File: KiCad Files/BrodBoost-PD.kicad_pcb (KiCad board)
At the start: 4 copper layers, 54 x 11.6 mm, 39 parts, among them IC1 CYPD3177, J1 Conn_02x02_Counter_Clockwise, J2 Conn_02x02_Counter_Clockwise, J4 Conn_01x02_Pin, J6 Output, P1 USB Type C, Q2 DMP3013, Q3 DMP3013, SW1 SW_DIP_x05

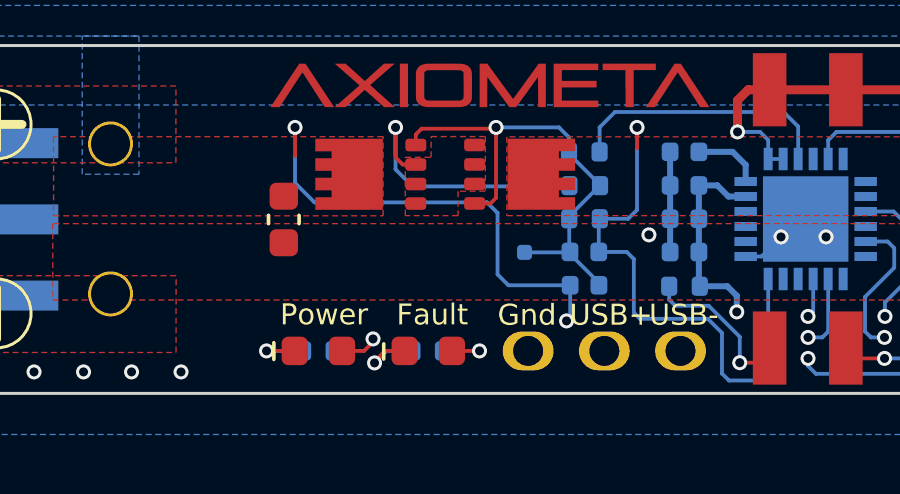
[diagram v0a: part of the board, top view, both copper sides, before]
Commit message: almost finished husb238 version
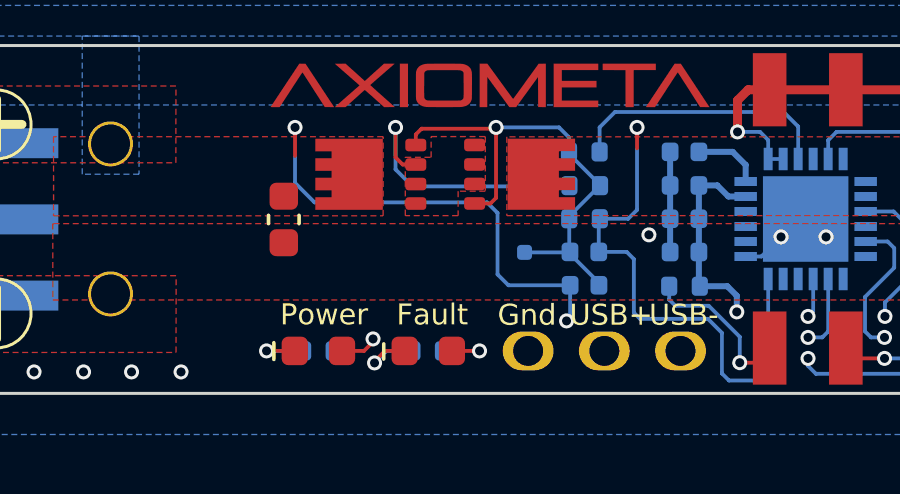
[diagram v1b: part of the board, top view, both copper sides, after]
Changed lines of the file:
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@@
 	)
 	(gr_text "Fault"
-		(at 145.684178 106.94975 0)
+		(at 145.683178 106.94975 0)
 		(layer "F.SilkS")
 		(effects
@@
 			(polygon
 				(pts
-					(xy 145.757438 106.83075) (xy 145.757438 106.144732) (xy 146.174904 106.144732) (xy 146.174904 106.212351)
-					(xy 145.83976 106.212351) (xy 145.83976 106.453461) (xy 146.124938 106.453461) (xy 146.124938 106.520097)
-					(xy 145.83976 106.520097) (xy 145.83976 106.83075)
+					(xy 145.756438 106.83075) (xy 145.756438 106.144732) (xy 146.173904 106.144732) (xy 146.173904 106.212351)
+					(xy 145.83876 106.212351) (xy 145.83876 106.453461) (xy 146.123938 106.453461) (xy 146.123938 106.520097)
+					(xy 145.83876 106.520097) (xy 145.83876 106.83075)
 				)
 			)
 			(polygon
 				(pts
-					(xy 146.489112 106.328633) (xy 146.526534 106.337184) (xy 146.557791 106.35058) (xy 146.58581 106.369598)
-					(xy 146.608342 106.392654) (xy 146.625923 106.420122) (xy 146.638219 106.450617) (xy 146.645892 106.485245)
-					(xy 146.648576 106.524756) (xy 146.648576 106.83075) (xy 146.575102 106.83075) (xy 146.570187 106.743298)
-					(xy 146.559099 106.763159) (xy 146.545182 106.78198) (xy 146.528802 106.798869) (xy 146.509792 106.813482)
-					(xy 146.488409 106.825273) (xy 146.463245 106.834639) (xy 146.435958 106.840448) (xy 146.404089 106.842504)
-					(xy 146.364321 106.839929) (xy 146.331287 106.832749) (xy 146.303858 106.82156) (xy 146.278998 106.805655)
-					(xy 146.259361 106.787087) (xy 146.244318 106.765695) (xy 146.229654 106.729414) (xy 146.224742 106.690127)
-					(xy 146.22511 106.686194) (xy 146.310996 106.686194) (xy 146.314118 106.711116) (xy 146.323092 106.732014)
-					(xy 146.337866 106.749159) (xy 146.358996 106.762276) (xy 146.38431 106.770077) (xy 146.41657 106.772919)
-					(xy 146.449807 106.769252) (xy 146.478932 106.7586) (xy 146.504705 106.741724) (xy 146.526461 106.719662)
-					(xy 146.543714 106.693581) (xy 146.55621 106.664396) (xy 146.563733 106.633272) (xy 146.566254 106.600923)
-					(xy 146.566254 106.59776) (xy 146.442558 106.59776) (xy 146.3975 106.600934) (xy 146.365749 106.609172)
-					(xy 146.339845 106.623264) (xy 146.323734 106.640503) (xy 146.314247 106.66167) (xy 146.310996 106.686194)
-					(xy 146.22511 106.686194) (xy 146.227793 106.657509) (xy 146.236518 106.629517) (xy 146.250687 106.60524)
-					(xy 146.269869 106.584416) (xy 146.294064 106.566784) (xy 146.324075 106.552325) (xy 146.37404 106.538912)
-					(xy 146.435676 106.534074) (xy 146.566254 106.534074) (xy 146.562467 106.490063) (xy 146.552278 106.457009)
-					(xy 146.534836 106.429819) (xy 146.511159 106.410676) (xy 146.481851 106.399246) (xy 146.444267 106.395118)
-					(xy 146.41363 106.397861) (xy 146.386741 106.405766) (xy 146.362886 106.418669) (xy 146.343166 106.43653)
-					(xy 146.329199 106.459111) (xy 146.320784 106.487484) (xy 146.236496 106.487484) (xy 146.24331 106.453654)
-					(xy 146.255268 106.424476) (xy 146.272272 106.399178) (xy 146.293785 106.377289) (xy 146.318875 106.35908)
-					(xy 146.347968 106.344425) (xy 146.394844 106.33031) (xy 146.444267 106.325576)
+					(xy 146.488112 106.328633) (xy 146.525534 106.337184) (xy 146.556791 106.35058) (xy 146.58481 106.369598)
+					(xy 146.607342 106.392654) (xy 146.624923 106.420122) (xy 146.637219 106.450617) (xy 146.644892 106.485245)
+					(xy 146.647576 106.524756) (xy 146.647576 106.83075) (xy 146.574102 106.83075) (xy 146.569187 106.743298)
+					(xy 146.558099 106.763159) (xy 146.544182 106.78198) (xy 146.527802 106.798869) (xy 146.508792 106.813482)
+					(xy 146.487409 106.825273) (xy 146.462245 106.834639) (xy 146.434958 106.840448) (xy 146.403089 106.842504)
+					(xy 146.363321 106.839929) (xy 146.330287 106.832749) (xy 146.302858 106.82156) (xy 146.277998 106.805655)
+					(xy 146.258361 106.787087) (xy 146.243318 106.765695) (xy 146.228654 106.729414) (xy 146.223742 106.690127)
+					(xy 146.22411 106.686194) (xy 146.309996 106.686194) (xy 146.313118 106.711116) (xy 146.322092 106.732014)
+					(xy 146.336866 106.749159) (xy 146.357996 106.762276) (xy 146.38331 106.770077) (xy 146.41557 106.772919)
+					(xy 146.448807 106.769252) (xy 146.477932 106.7586) (xy 146.503705 106.741724) (xy 146.525461 106.719662)
+					(xy 146.542714 106.693581) (xy 146.55521 106.664396) (xy 146.562733 106.633272) (xy 146.565254 106.600923)
+					(xy 146.565254 106.59776) (xy 146.441558 106.59776) (xy 146.3965 106.600934) (xy 146.364749 106.609172)
+					(xy 146.338845 106.623264) (xy 146.322734 106.640503) (xy 146.313247 106.66167) (xy 146.309996 106.686194)
+					(xy 146.22411 106.686194) (xy 146.226793 106.657509) (xy 146.235518 106.629517) (xy 146.249687 106.60524)
+					(xy 146.268869 106.584416) (xy 146.293064 106.566784) (xy 146.323075 106.552325) (xy 146.37304 106.538912)
+					(xy 146.434676 106.534074) (xy 146.565254 106.534074) (xy 146.561467 106.490063) (xy 146.551278 106.457009)
+					(xy 146.533836 106.429819) (xy 146.510159 106.410676) (xy 146.480851 106.399246) (xy 146.443267 106.395118)
+					(xy 146.41263 106.397861) (xy 146.385741 106.405766) (xy 146.361886 106.418669) (xy 146.342166 106.43653)
+					(xy 146.328199 106.459111) (xy 146.319784 106.487484) (xy 146.235496 106.487484) (xy 146.24231 106.453654)
+					(xy 146.254268 106.424476) (xy 146.271272 106.399178) (xy 146.292785 106.377289) (xy 146.317875 106.35908)
+					(xy 146.346968 106.344425) (xy 146.393844 106.33031) (xy 146.443267 106.325576)
 				)
 			)
 			(polygon
 				(pts
-					(xy 146.954698 106.842504) (xy 146.917387 106.839835) (xy 146.884511 106.83218) (xy 146.855365 106.81985)
-					(xy 146.829401 106.802267) (xy 146.807601 106.77935) (xy 146.789669 106.750394) (xy 146.777354 106.718358)
-					(xy 146.769407 106.679527) (xy 146.766546 106.632553) (xy 146.766546 106.33733) (xy 146.848868 106.33733)
-					(xy 146.848868 106.623705) (xy 146.853035 106.672157) (xy 146.864211 106.708251) (xy 146.881181 106.734878)
-					(xy 146.905047 106.755015) (xy 146.93512 106.767474) (xy 146.973291 106.771936) (xy 147.012741 106.766862)
-					(xy 147.047449 106.751975) (xy 147.067622 106.736895) (xy 147.084926 106.717739) (xy 147.09951 106.693974)
-					(xy 147.10977 106.667907) (xy 147.116295 106.637183) (xy 147.118616 106.600923) (xy 147.118616 106.33733)
-					(xy 147.200938 106.33733) (xy 147.200938 106.83075) (xy 147.126438 106.83075) (xy 147.121565 106.744752)
-					(xy 147.103949 106.773171) (xy 147.081786 106.796963) (xy 147.054673 106.816559) (xy 147.024341 106.830835)
-					(xy 146.991225 106.839522)
+					(xy 146.953698 106.842504) (xy 146.916387 106.839835) (xy 146.883511 106.83218) (xy 146.854365 106.81985)
+					(xy 146.828401 106.802267) (xy 146.806601 106.77935) (xy 146.788669 106.750394) (xy 146.776354 106.718358)
+					(xy 146.768407 106.679527) (xy 146.765546 106.632553) (xy 146.765546 106.33733) (xy 146.847868 106.33733)
+					(xy 146.847868 106.623705) (xy 146.852035 106.672157) (xy 146.863211 106.708251) (xy 146.880181 106.734878)
+					(xy 146.904047 106.755015) (xy 146.93412 106.767474) (xy 146.972291 106.771936) (xy 147.011741 106.766862)
+					(xy 147.046449 106.751975) (xy 147.066622 106.736895) (xy 147.083926 106.717739) (xy 147.09851 106.693974)
+					(xy 147.10877 106.667907) (xy 147.115295 106.637183) (xy 147.117616 106.600923) (xy 147.117616 106.33733)
+					(xy 147.199938 106.33733) (xy 147.199938 106.83075) (xy 147.125438 106.83075) (xy 147.120565 106.744752)
+					(xy 147.102949 106.773171) (xy 147.080786 106.796963) (xy 147.053673 106.816559) (xy 147.023341 106.830835)
+					(xy 146.990225 106.839522)
 				)
 			)
 			(polygon
 				(pts
-					(xy 147.336859 106.83075) (xy 147.336859 106.125156) (xy 147.419138 106.125156) (xy 147.419138 106.83075)
+					(xy 147.335859 106.83075) (xy 147.335859 106.125156) (xy 147.418138 106.125156) (xy 147.418138 106.83075)
 				)
 			)
 			(polygon
 				(pts
-					(xy 147.749025 106.83075) (xy 147.70675 106.827118) (xy 147.672559 106.817029) (xy 147.652787 106.805821)
-					(xy 147.636416 106.790479) (xy 147.623105 106.770483) (xy 147.614124 106.74791) (xy 147.608164 106.718853)
-					(xy 147.605966 106.681792) (xy 147.605966 106.406915) (xy 147.520224 106.406915) (xy 147.520224 106.33733)
-					(xy 147.605966 106.33733) (xy 147.616737 106.217779) (xy 147.688288 106.217779) (xy 147.688288 106.33733)
-					(xy 147.832074 106.33733) (xy 147.832074 106.406915) (xy 147.688288 106.406915) (xy 147.688288 106.681792)
-					(xy 147.690883 106.712046) (xy 147.697454 106.731746) (xy 147.706881 106.744025) (xy 147.720424 106.752183)
-					(xy 147.741377 106.757926) (xy 147.772576 106.760182) (xy 147.825705 106.760182) (xy 147.825705 106.83075)
+					(xy 147.748025 106.83075) (xy 147.70575 106.827118) (xy 147.671559 106.817029) (xy 147.651787 106.805821)
+					(xy 147.635416 106.790479) (xy 147.622105 106.770483) (xy 147.613124 106.74791) (xy 147.607164 106.718853)
+					(xy 147.604966 106.681792) (xy 147.604966 106.406915) (xy 147.519224 106.406915) (xy 147.519224 106.33733)
+					(xy 147.604966 106.33733) (xy 147.615737 106.217779) (xy 147.687288 106.217779) (xy 147.687288 106.33733)
+					(xy 147.831074 106.33733) (xy 147.831074 106.406915) (xy 147.687288 106.406915) (xy 147.687288 106.681792)
+					(xy 147.689883 106.712046) (xy 147.696454 106.731746) (xy 147.705881 106.744025) (xy 147.719424 106.752183)
+					(xy 147.740377 106.757926) (xy 147.771576 106.760182) (xy 147.824705 106.760182) (xy 147.824705 106.83075)
 				)
 			)
